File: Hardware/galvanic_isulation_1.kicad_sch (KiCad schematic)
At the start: 14 parts

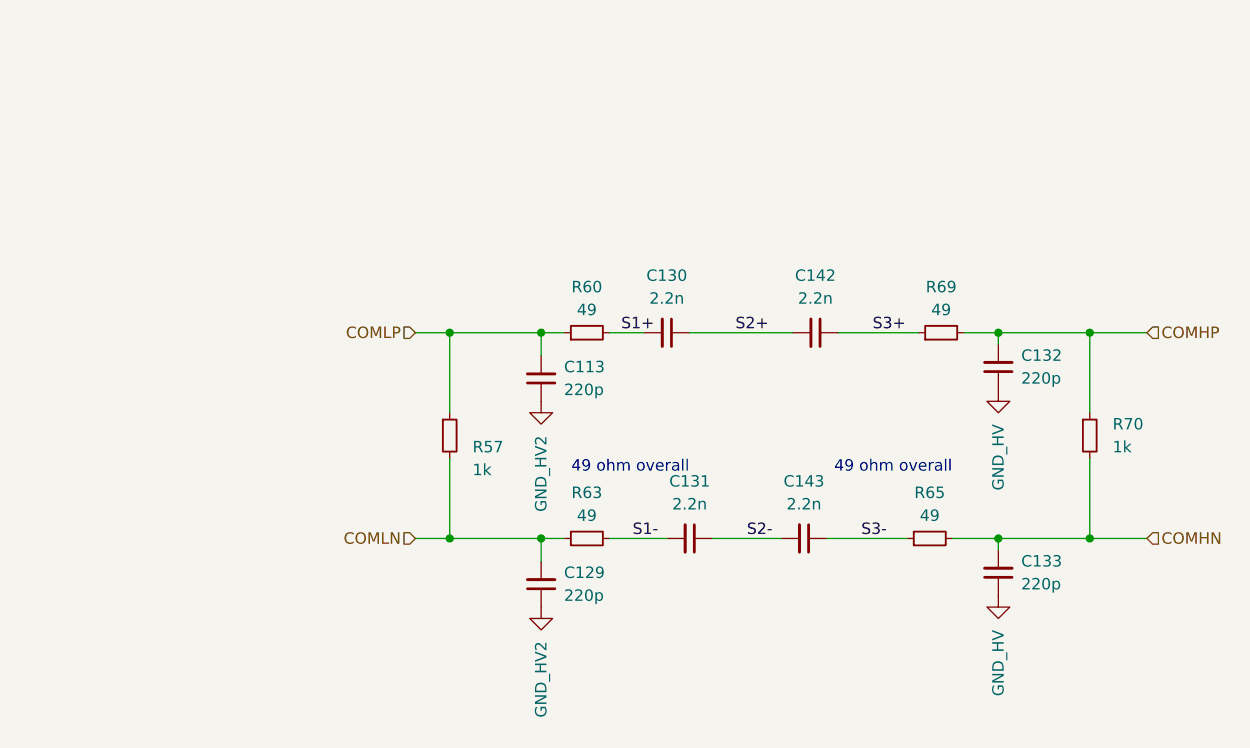
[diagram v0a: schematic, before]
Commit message: Zmiany wizualne w schemacie
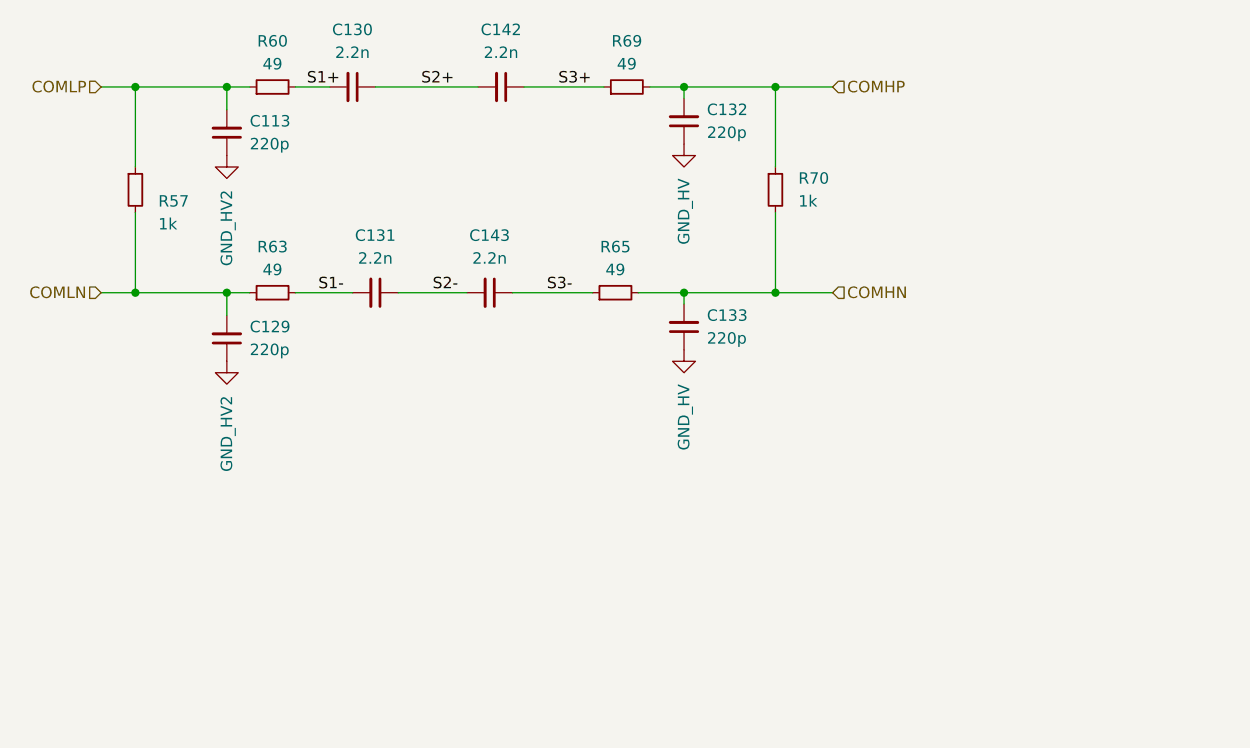
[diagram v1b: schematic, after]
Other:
- note removed: "49 ohm overall"
- moved on the sheet: C113, C129, C130, C131, C132, C133, C142, C143, R57, R60, R63, R65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
